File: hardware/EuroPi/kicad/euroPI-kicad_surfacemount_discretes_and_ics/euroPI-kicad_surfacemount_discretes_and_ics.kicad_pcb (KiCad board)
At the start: 2 copper layers, 121.9 x 128.5 mm, 104 parts, among them J1 Output 1 Jack, J10 Eurorack Power 2x8 16p, J11 Conn_01x13_Socket, J12 OLED 64x128, J13 USB_B_Micro, J14 Conn_01x03_Pin, J15 Conn_01x04_Pin, J16 Conn_02x04_Top_Bottom, J17 Conn_01x13_Pin, J18 Conn_01x04_Pin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

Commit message: kicad smd :)
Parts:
- D1, D2, D3, D4: value type="D" model="DIODE" lib="" -> 1N4448W; footprint Diode_SMD:D_0805_2012Metric_Pad1.15x1.40mm_HandSolder -> Diode_SMD:D_SOD-123
- Q1: footprint Package_TO_SOT_SMD:SOT-23 -> Package_TO_SOT_THT:TO-92
- U1: footprint Package_TO_SOT_SMD:TO-252-3_TabPin2 -> Package_TO_SOT_THT:TO-220-3_Vertical; moved to B.Cu
- moved J20 11.9 mm to (112.8, 139.8), turned to 0 degrees
- moved U1 9.62 mm to (180.3, 29.5)
- moved O3 8.83 mm to (170.5, 113.4)
- moved O5 8.83 mm to (182.2, 113.4)
- moved R21 8.83 mm to (185.0, 119.5)
- moved R22 8.83 mm to (189.3, 119.5)
- moved R29 8.83 mm to (172.0, 119.5)
- moved R35 8.83 mm to (167.7, 119.5)
- moved R36 8.83 mm to (176.3, 119.5)
- moved R30 8.83 mm to (180.6, 119.5)
- moved R39 8.70 mm to (171.0, 99.5)
- moved D2 8.58 mm to (178.3, 58.5)
- moved D1 8.53 mm to (169.1, 58.6)
- moved C10 8.52 mm to (190.2, 93.1)
- moved C11 8.52 mm to (190.2, 106.0)
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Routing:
- net CJ3: track 97.3 -> 60.1 mm, vias 4 -> 2
- net I2C_GND: track 868.1 -> 845.6 mm
- net Net-(LED7-K): track 21.3 -> 8.11 mm
- net ~: track 140.3 -> 153.1 mm
- net CS1: track 58.7 -> 66.0 mm
- net CJD: track 43.7 -> 49.2 mm
- net Net-(O5C--): track 23.7 -> 28.1 mm
- net Net-(LED7-A): track 9.63 -> 13.7 mm
- net Net-(O3D--): track 14.0 -> 11.4 mm
- net CJ6: track 123.5 -> 121.0 mm
- net Net-(O3C-+): track 26.6 -> 24.2 mm
- net CJ1: track 58.8 -> 56.4 mm
- net CJ4: track 89.4 -> 87.2 mm
- net Net-(C18-Pad1): track 11.8 -> 13.9 mm
- net GP22: track 32.6 -> 30.6 mm
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
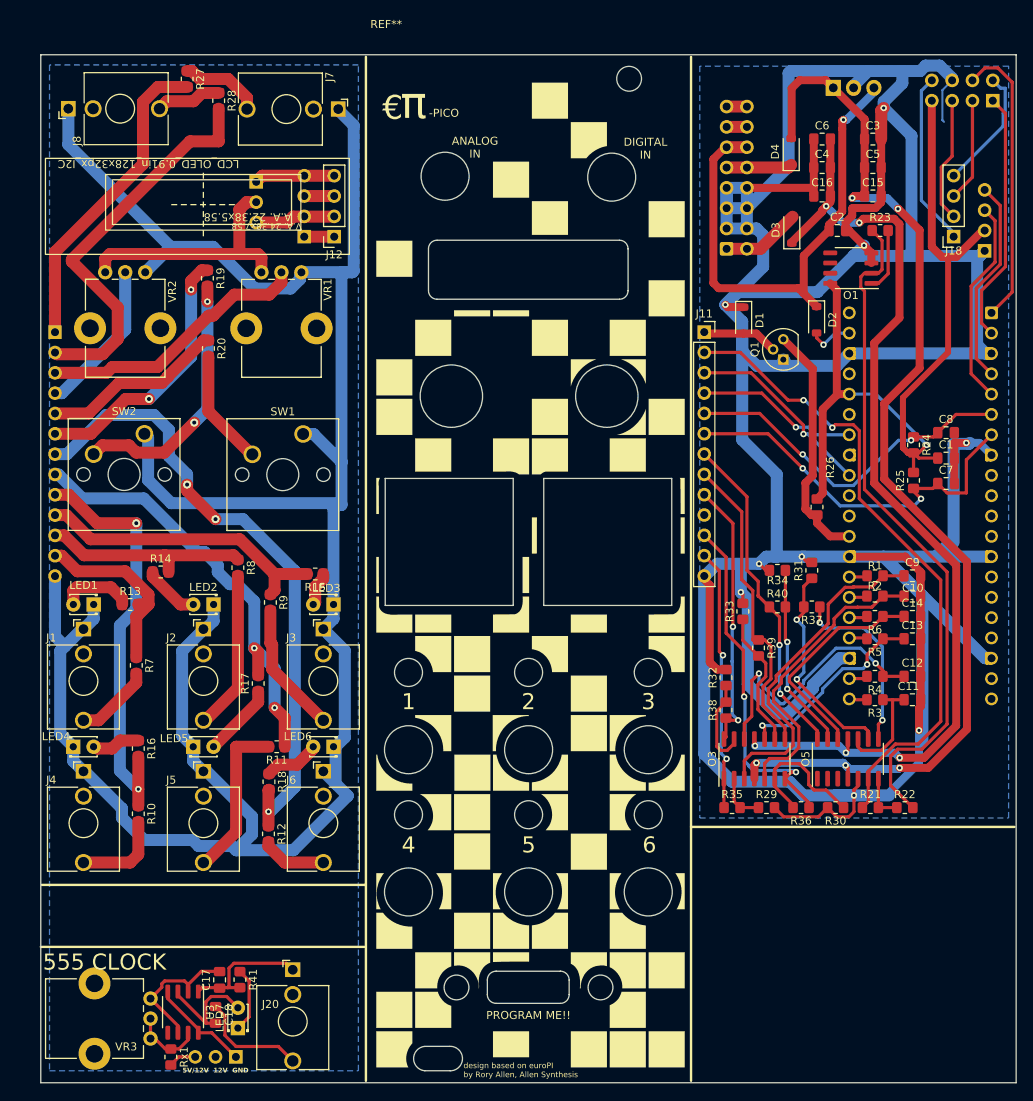
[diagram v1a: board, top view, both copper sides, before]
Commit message: THT version updated with ground plane
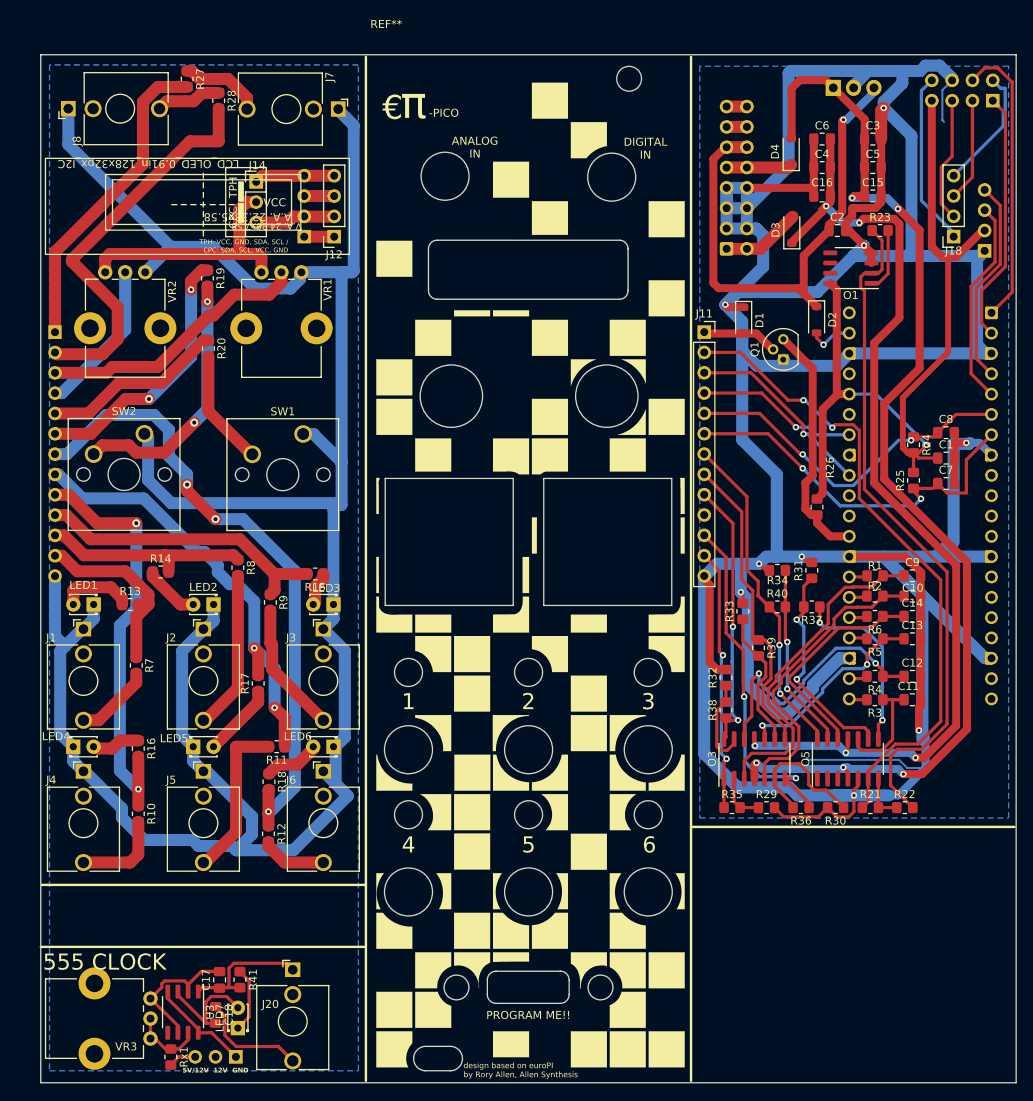
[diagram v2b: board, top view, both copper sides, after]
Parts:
- J14: moved to F.Cu
- turned J14 to 0 degrees
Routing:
- net I2C_GND: track 845.6 -> 862.5 mm
- net ~: track 153.1 -> 154.0 mm

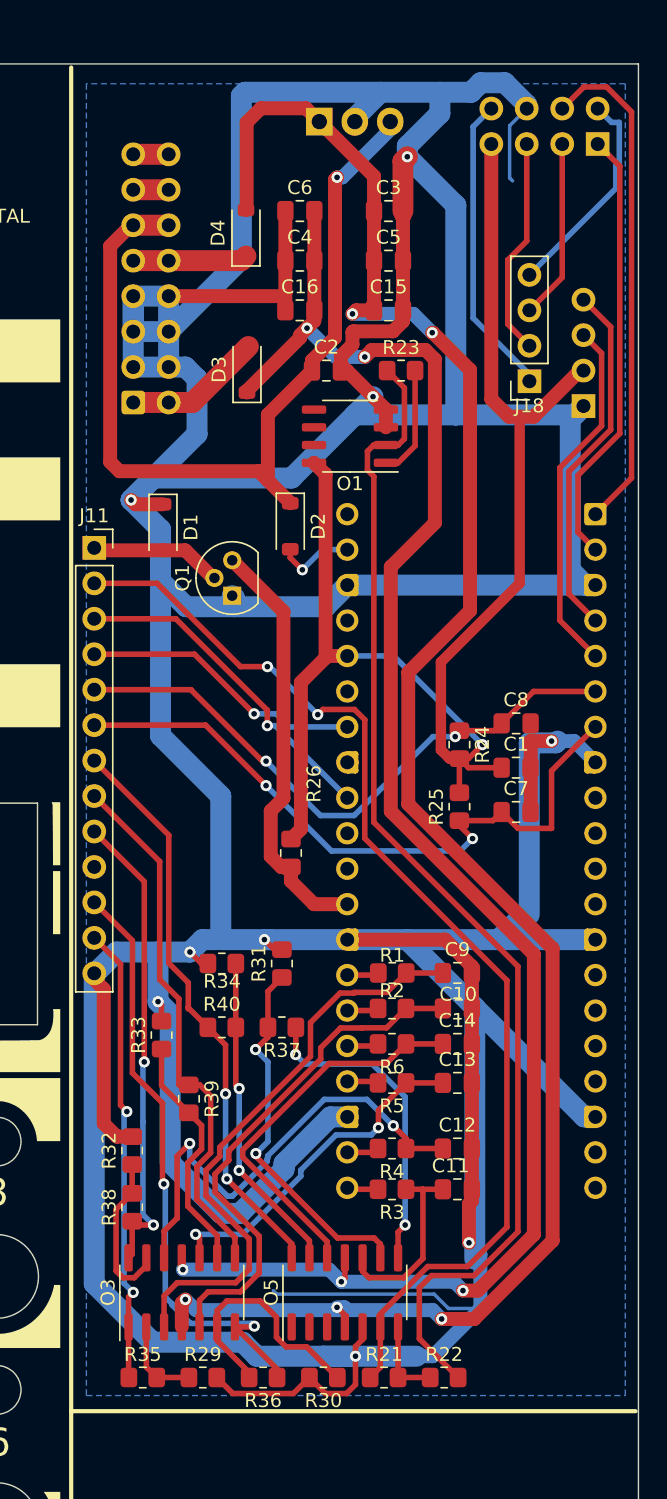
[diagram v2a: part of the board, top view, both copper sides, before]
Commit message: misc improvements THT fixed grounds and misc clean up issue likely still wtih usb output SMT redid caps to be near to necessary fixed GND and misc things to make it easier to hand solder
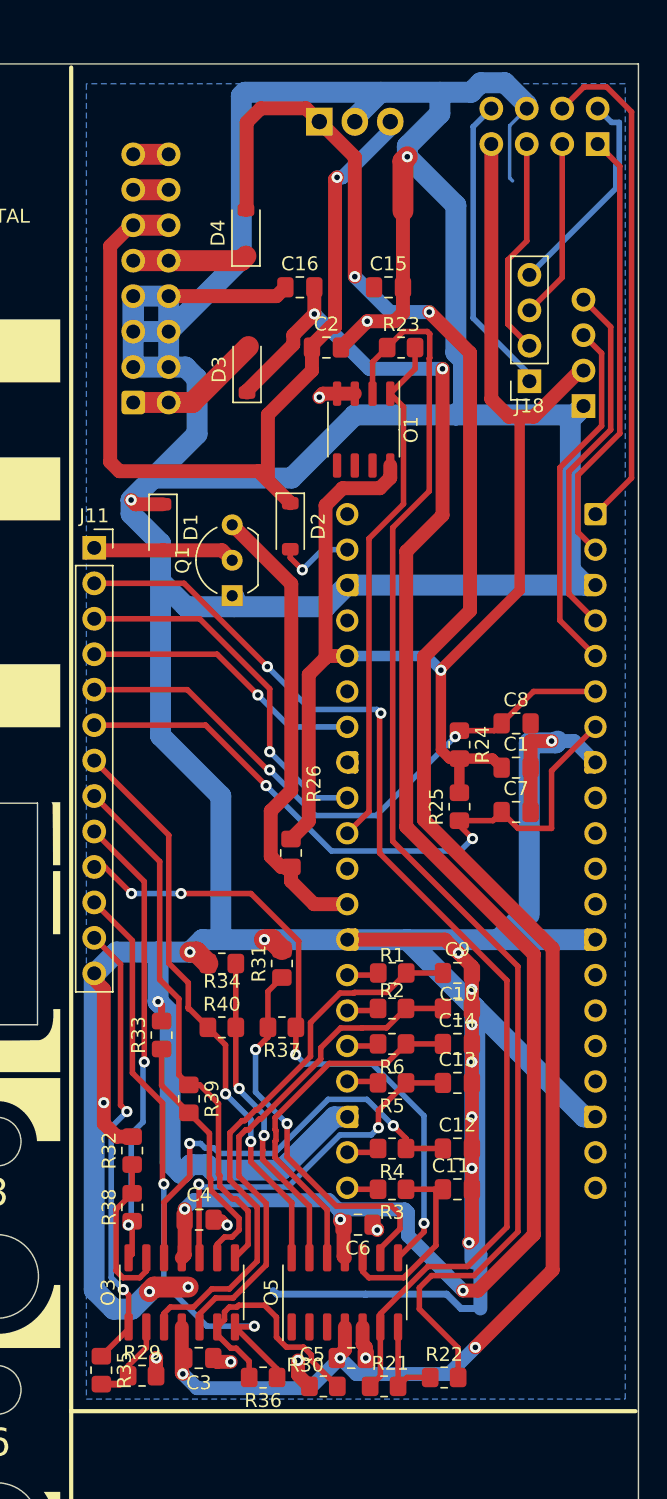
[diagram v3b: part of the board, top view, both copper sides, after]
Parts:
- Q1: footprint Package_TO_SOT_THT:TO-92 -> Package_TO_SOT_THT:TO-92_Inline_Wide
- moved C3 83.3 mm to (171.7, 118.1)
- moved C5 78.7 mm to (182.6, 118.1)
- moved C6 72.7 mm to (183.1, 108.6), turned to 180 degrees
- moved C4 69.1 mm to (171.7, 108.2), turned to 180 degrees
- moved R29 4.35 mm to (167.6, 119.4)
- moved R35 3.02 mm to (164.7, 119.0), turned to -90 degrees
- moved C2 1.65 mm to (180.8, 45.7)
- moved R23 1.65 mm to (186.2, 45.7)
- moved C15 1.65 mm to (185.3, 41.4)
- moved C16 1.65 mm to (178.9, 41.4)
- moved O1 1.09 mm to (183.5, 51.6), turned to -90 degrees
- moved R21 0.63 mm to (185.0, 120.1)
- moved R30 0.63 mm to (180.6, 120.1)
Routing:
- net I2C_GND: track 862.5 -> 810.0 mm, vias 9 -> 24
- net GP26: track 7.98 -> 37.6 mm
- net CJ3: track 60.1 -> 84.4 mm, vias 2 -> 4
- net Net-(O1A--): track 85.1 -> 92.8 mm
- net I2C_VCC: track 136.1 -> 131.8 mm
- net Net-(O3D-+): track 33.3 -> 29.9 mm
- net GP22: track 30.6 -> 33.6 mm
- net Net-(O3C-+): track 24.2 -> 26.2 mm
- net -12V: track 123.1 -> 125.1 mm
- net CK1: track 58.3 -> 60.3 mm
- net Net-(O5D-+): track 27.1 -> 25.3 mm
- net Net-(O3A-+): track 41.5 -> 40.0 mm
- net Net-(O3B-+): track 36.9 -> 35.5 mm
- net CJA: track 130.4 -> 131.7 mm
- net ~: track 154.0 -> 155.3 mm
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
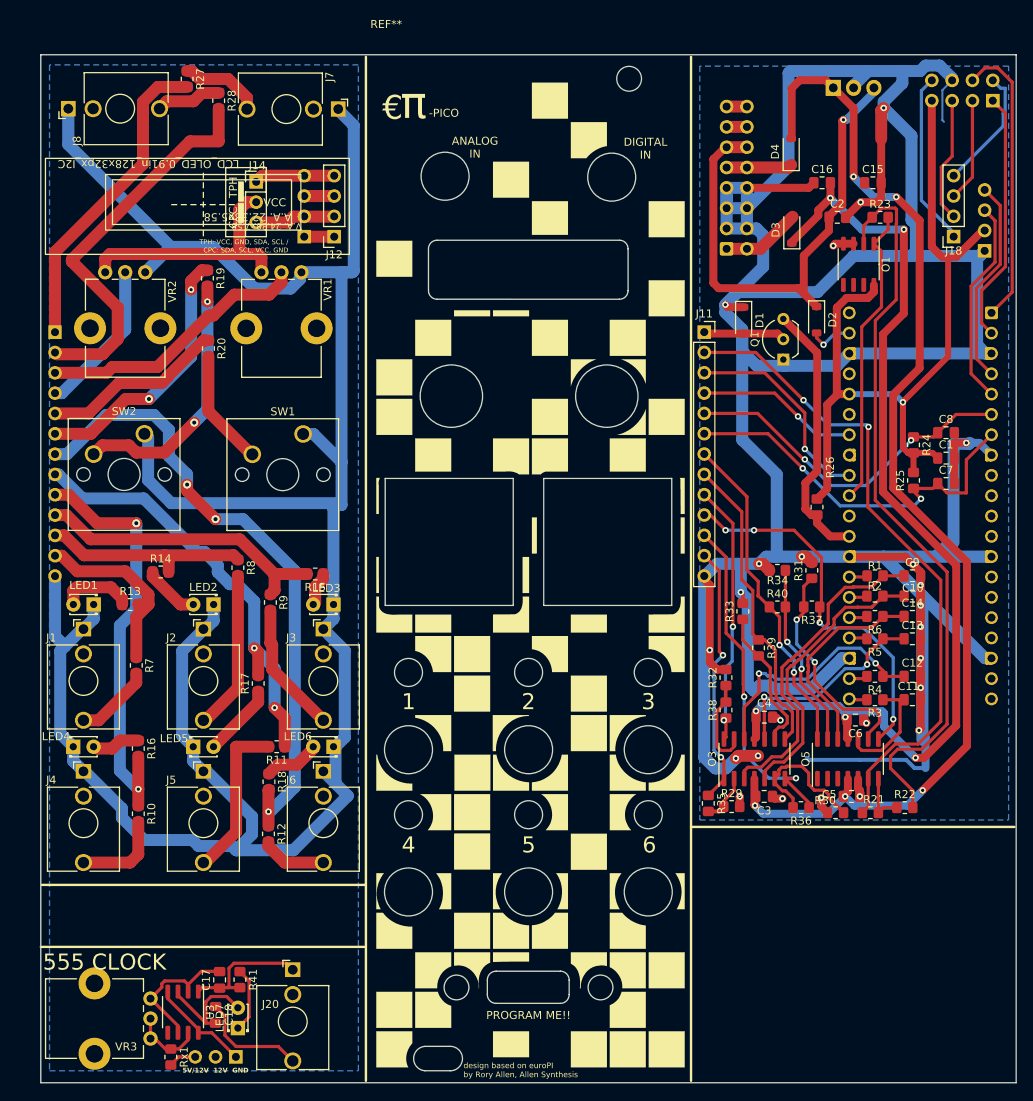
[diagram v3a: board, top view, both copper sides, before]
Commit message: smt updated and improved, gerbers updated and zipped todo fix proto board errors todo fix nets between boards
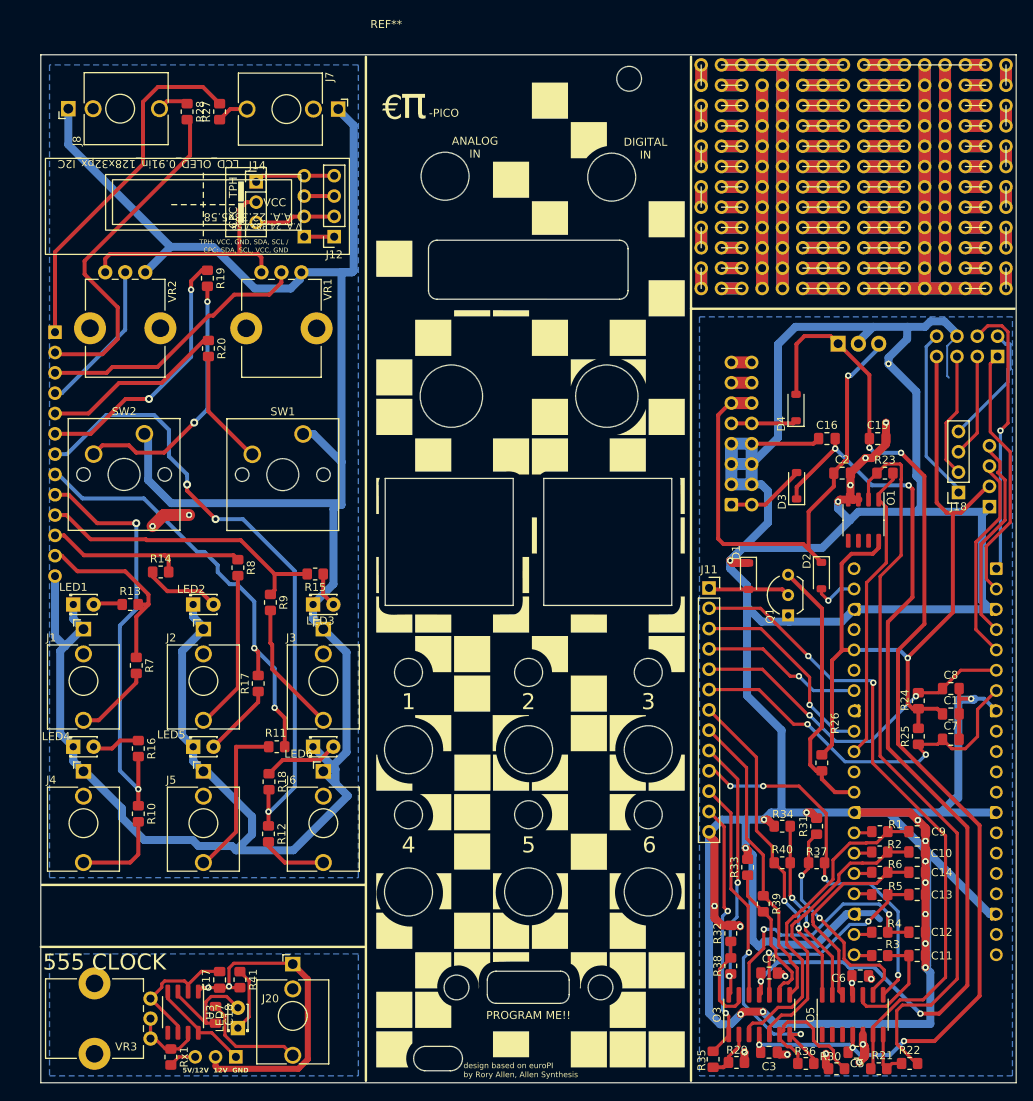
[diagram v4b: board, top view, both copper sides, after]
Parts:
- added REF**: protoPCB_45x70mm_16x26pins_2.54pitch 50%, Library:protoPCB_45x70mm_16x26pins_2.54pitch, F.Cu at (184.2, 59.7)
- moved R21 32.0 mm to (186.0, 152.1)
- moved R30 32.0 mm to (180.7, 152.1)
- moved R29 32.0 mm to (168.2, 151.4)
- moved C1 32.0 mm to (195.0, 107.8)
- moved C11 32.0 mm to (190.8, 138.0)
- moved C12 32.0 mm to (190.8, 135.1)
- moved C14 32.0 mm to (190.8, 127.6)
- moved C15 32.0 mm to (185.9, 73.4)
- moved C16 32.0 mm to (179.5, 73.4)
- moved C2 32.0 mm to (181.4, 77.7)
- moved C3 32.0 mm to (172.3, 150.1)
- moved C4 32.0 mm to (172.3, 140.2)
- moved C5 32.0 mm to (183.2, 150.1)
- moved C6 32.0 mm to (183.7, 140.5)
- moved C7 32.0 mm to (195.0, 111.0)
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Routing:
- net (no net): track 0.00 -> 675.7 mm, vias 0 -> 2
- net I2C_GND: track 810.0 -> 849.1 mm, vias 24 -> 30
- net Net-(J7-PadT): track 10.3 -> 3.98 mm
- net CJA: track 131.7 -> 125.5 mm
- net Net-(LED1-A): track 9.35 -> 3.68 mm
- net CJD: track 49.9 -> 54.8 mm
- net Net-(J8-PadT): track 8.21 -> 3.95 mm
- net -12V: track 125.1 -> 129.2 mm
- net Net-(LED2-A): track 7.09 -> 9.62 mm
- net Net-(LED6-A): track 7.08 -> 9.45 mm
- net Net-(O3D-+): track 29.9 -> 32.0 mm
- net ~: track 155.3 -> 154.0 mm
- net GP0: track 36.2 -> 34.9 mm, vias 0 -> 1
- net Net-(O1A--): track 92.8 -> 93.6 mm
- net Net-(O5C-+): track 13.5 -> 14.3 mm
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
